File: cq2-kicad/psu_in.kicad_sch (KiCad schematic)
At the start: 40 parts, among them Q1 XPH4R10, Q2 XPH4R10, U20 LM74700, U21 TLV1702, U22 TL431I, U23 100 %

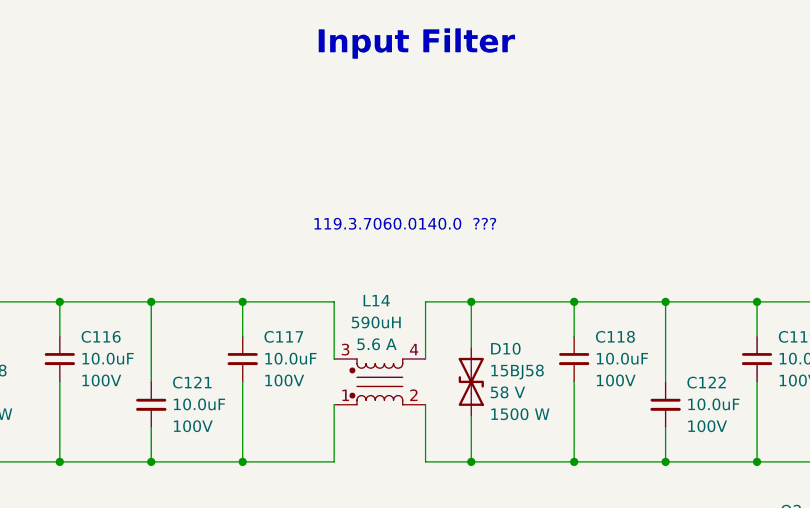
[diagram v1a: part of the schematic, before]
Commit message: Production documents created
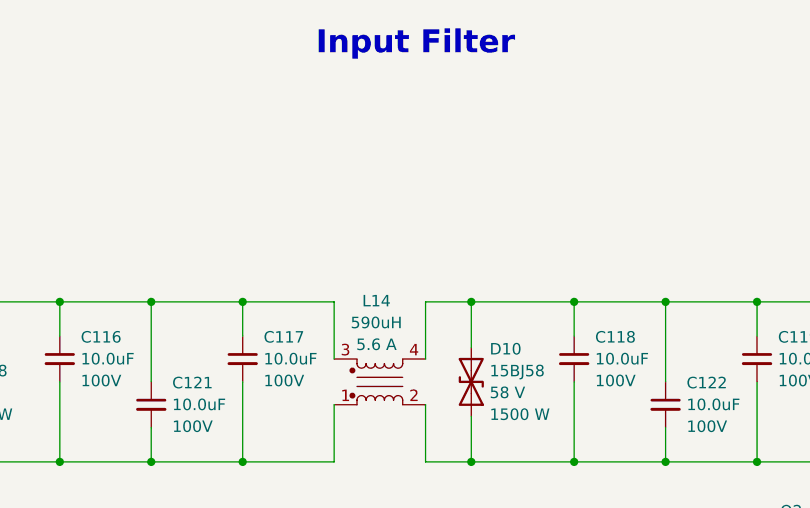
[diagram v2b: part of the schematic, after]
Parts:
- L14: MPN Pulse P0353NL -> Pulse P0353NLT; Outline (none) -> SMT 19.56x17.02x9.91mm
- Q1, Q2: Outline (none) -> SMT SOP-Advance-8
- U20, U22: Outline (none) -> SMT SOT-23
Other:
- note removed: "119.3.7060.0140.0 ???"
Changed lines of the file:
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@@
 	(title_block
 		(title "CQ2")
-		(date "2024-07-31")
+		(date "2024-08-03")
 		(rev "0")
 		(comment 1 "Power Filter and Supervisor")
@@
 		)
 	)
-	(text "119.3.7060.0140.0  ???"
-		(exclude_from_sim no)
-		(at 119.634 46.228 0)
-		(effects
-			(font
-				(size 1.27 1.27)
-			)
-		)
-	)
 	(text "Reverse Polarity Protection"
 		(exclude_from_sim no)
@@
 			)
 		)
-		(property "Description" "Transistor MOSFET N-Channel - SMT"
+		(property "Description" "Transistor MOSFET N-Channel"
 			(at 162.56 88.9 0)
 			(effects
@@
 			)
 		)
-		(property "Outline" ""
+		(property "Outline" "SMT SOP-Advance-8"
 			(at 162.56 88.9 0)
 			(effects
@@
 			)
 		)
-		(property "Outline" ""
+		(property "Outline" "SMT SOT-23"
 			(at 223.52 57.15 0)
 			(effects
@@
 			)
 		)
-		(property "Description" "Analog Voltage Reference - SMT"
+		(property "Description" "Analog Voltage Reference"
 			(at 162.56 104.14 0)
 			(effects
@@
 			)
 		)
-		(property "Outline" ""
+		(property "Outline" "SMT SOT-23"
 			(at 162.56 104.14 0)
 			(effects
@@
 			)
 		)
-		(property "Description" "Common Mode Filter - SMT"
+		(property "Description" "Common Mode Filter"
 			(at 116.84 63.5 0)
 			(effects
@@
 			)
 		)
-		(property "MPN" "Pulse  P0353NL"
+		(property "MPN" "Pulse  P0353NLT"
 			(at 116.84 63.5 0)
 			(effects
@@
 			)
 		)
-		(property "Outline" ""
+		(property "Outline" "SMT 19.56x17.02x9.91mm"
 			(at 116.84 63.5 0)
 			(effects
@@
 			)
 		)
-		(property "Description" "Transistor MOSFET N-Channel - SMT"
+		(property "Description" "Transistor MOSFET N-Channel"
 			(at 224.79 40.64 0)
 			(effects
@@
 			)
 		)
-		(property "Outline" ""
+		(property "Outline" "SMT SOP-Advance-8"
 			(at 224.79 40.64 0)
 			(effects

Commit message: cq2 adapter in work
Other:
- note added: "Q2 Source und Drain vertauscht"
